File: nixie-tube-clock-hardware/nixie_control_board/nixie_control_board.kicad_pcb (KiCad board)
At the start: 2 copper layers, 52.5 x 97 mm, 67 parts, among them J1 Conn_01x07, J2 Conn_01x02_Female, P1 CONN_01X02, P2 CONN_01X02, P3 AMS1117, P4 CONN_01X02, P5 ., P6 CONN_01X02, P7 CONN_01X02, Q1 IRF644, Q2 Q_PNP_BEC, SW4 SW_DIP_x01, U1 DS3231, U2 AT24C02, U3 MAX1771, U5 DHT11, U6 Logo, U7 SSD1306-OLED, U8 MP2307

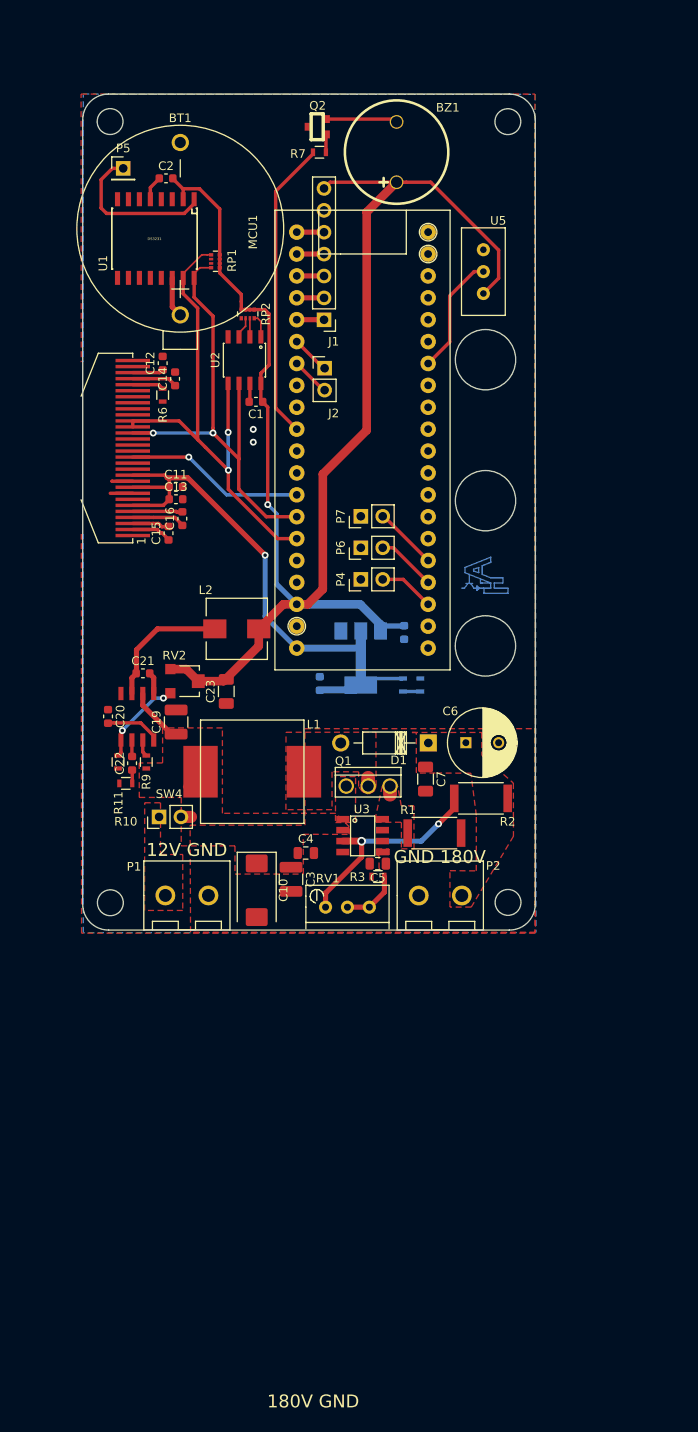
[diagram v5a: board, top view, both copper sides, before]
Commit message: Updated 180V boost supply and updated gitignore
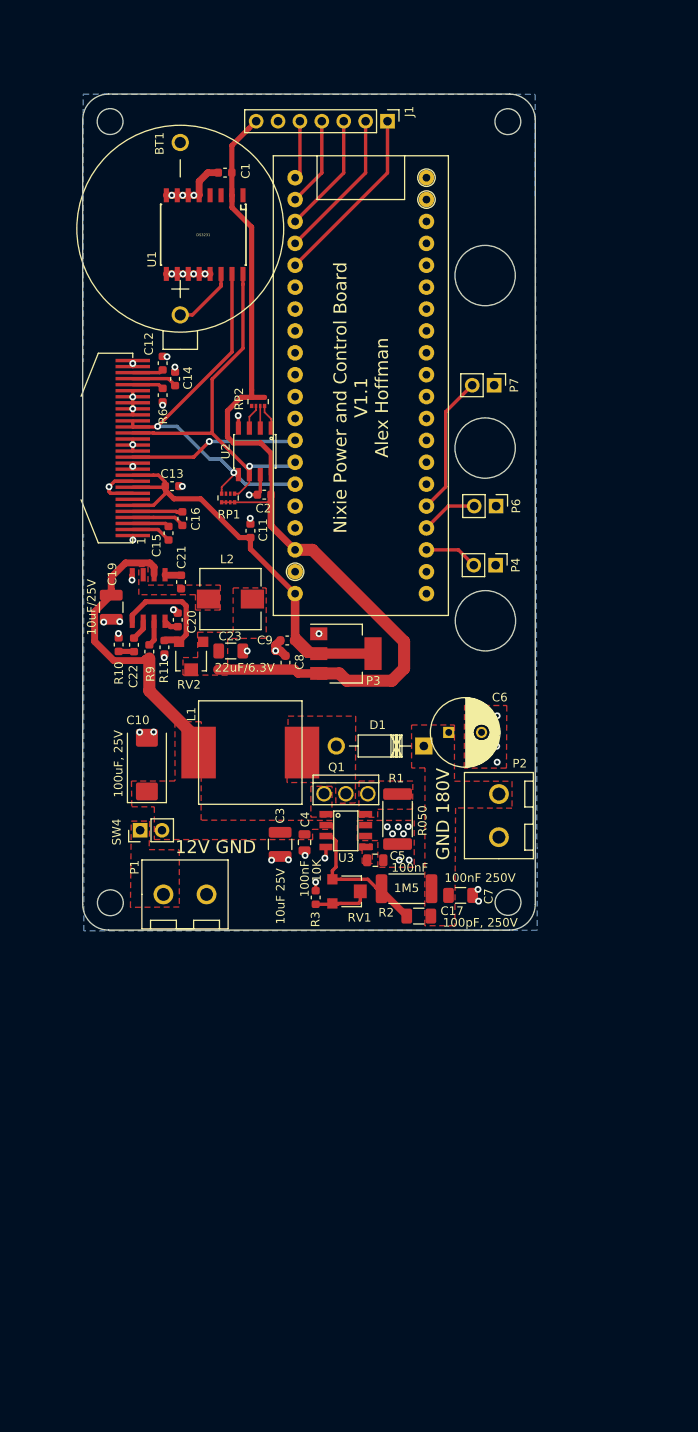
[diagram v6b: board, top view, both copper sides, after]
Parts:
- removed BZ1: Buzzer, keyboard:buzzer
- removed J2: Conn_01x02_Female, Connector_PinHeader_2.54mm:PinHeader_1x02_P2.54mm_Vertical
- removed P5: ., Connector_PinHeader_2.54mm:PinHeader_1x01_P2.54mm_Vertical
- removed Q2: Q_PNP_BEC, keyboard:SOT23-3
- removed R4, R5: 0, Resistors_SMD:R_0603
- removed R7: 1K, Resistors_SMD:R_0603
- removed U5: DHT11, keyboard:DHT11
- removed U6: Logo, keyboard:Logo
- added C17: 100pF, 250V, Capacitor_SMD:C_1206_3216Metric, F.Cu at (159.5, 145.4)
- C3: value 10uF, 25V -> 10uF 25V
- C7: value 100nF, 250V -> 100nF 250V
- C8, C9, P3: moved to F.Cu
- R1: footprint Resistors_SMD:R_2512 -> Resistor_SMD:R_2512_6332Metric
- R10, R11, R3, R6, R9: footprint Resistors_SMD:R_0603 -> Resistor_SMD:R_0603_1608Metric
- R2: value 1M5,220V -> 1M5; footprint Resistors_SMD:R_2512 -> Resistor_SMD:R_2512_6332Metric
- RV1: footprint Potentiometers:Potentiometer_Bourns_3296W_3-8Zoll_Inline_ScrewUp -> Potentiometer_SMD:Potentiometer_Trimmer-EVM3E
- RV2: footprint Potentiometers:Potentiometer_Trimmer-EVM3E -> Potentiometer_SMD:Potentiometer_Trimmer-EVM3E
- SW4: footprint Pin_Headers:Pin_Header_Straight_1x02_Pitch2.54mm -> Connector_PinHeader_2.54mm:PinHeader_1x02_P2.54mm_Vertical
- moved C2 38.4 mm to (141.6, 96.5)
- moved RP1 27.5 mm to (137.4, 96.9), turned to 90 degrees
- moved C1 26.8 mm to (137.0, 59.1)
- moved J1 24.2 mm to (155.9, 53.1), turned to 270 degrees
- moved P7 21.7 mm to (168.3, 83.8), turned to 270 degrees
- moved C10 19.4 mm to (128.0, 127.8), turned to 90 degrees
- moved P6 16.4 mm to (168.5, 97.8), turned to 270 degrees
- moved R10 16.1 mm to (124.7, 113.9), turned to 270 degrees
- moved P4 15.7 mm to (168.4, 104.7), turned to 270 degrees
- moved C19 15.3 mm to (123.8, 109.5), turned to 270 degrees
- moved R11 14.4 mm to (130.0, 114.2)
- moved C8 14.2 mm to (144.0, 116.0), turned to 90 degrees
- moved C7 14.1 mm to (164.4, 143.0), turned to 0 degrees
- moved U8 13.8 mm to (128.2, 108.5)
- moved C20 13.8 mm to (131.6, 111.0)
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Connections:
- MCU1 pad 31: BUZZER -> Net-(MCU1-Pad31)
- MCU1 pad 34: RX -> Net-(MCU1-Pad34)
- MCU1 pad 35: TX -> Net-(MCU1-Pad35)
- MCU1 pad 7: DHT -> Net-(MCU1-Pad7)
- RP1 pad 5: SDA -> SCL
- RP1 pad 8: SCL -> SDA
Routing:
- net +5V: track 178.7 -> 109.6 mm, vias 1 -> 0
- net BUZZER: track 34.9 -> 0.00 mm
- net GND: track 12.1 -> 43.0 mm, vias 2 -> 50
- net +12V: track 11.9 -> 34.5 mm
- net Net-(P5-Pad1): track 18.4 -> 0.00 mm
- net SHIFT_CLEAR: track 3.16 -> 21.2 mm
- net +3V3: track 68.8 -> 52.8 mm, vias 1 -> 0
- net Net-(C21-Pad1): track 15.4 -> 0.00 mm
- net SHIFT_OUT_ENABLE: track 3.16 -> 17.6 mm
- net SDA: track 60.9 -> 46.9 mm
- net DHT: track 13.9 -> 0.00 mm
- net SHIFT_LATCH_CLOCK: track 3.16 -> 14.0 mm
- net BUTTON_3: track 7.39 -> 16.2 mm
- net Net-(BZ1-Pad2): track 8.33 -> 0.00 mm
- net Net-(C17-Pad2): track 25.0 -> 16.8 mm, vias 2 -> 0
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- added copper zone on F.Cu, net +5V
- added copper zone on F.Cu, net Net-(C21-Pad1)
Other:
- board text added: "Nixie Power and Control Board V1.1 Alex Hoffman"
- board text removed: "180V GND"

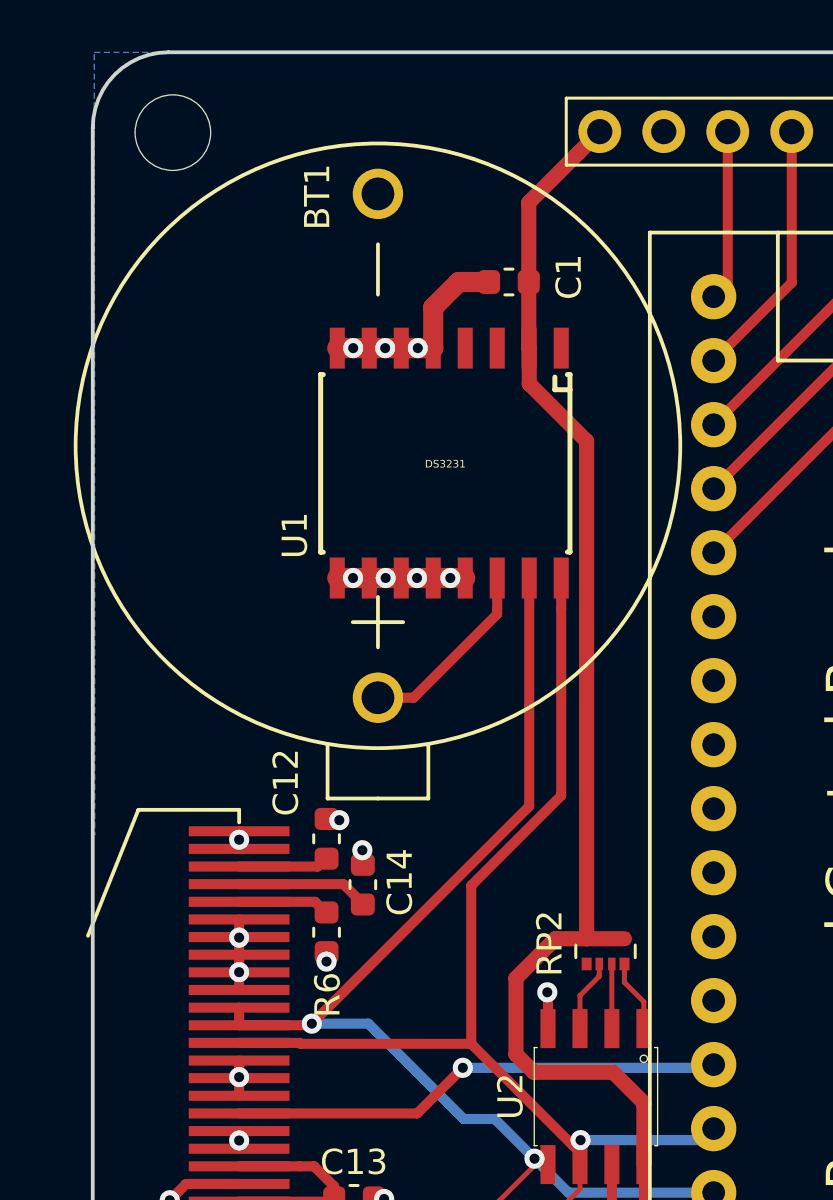
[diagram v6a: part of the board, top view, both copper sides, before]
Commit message: Added empty bluepill project and moved RT clock battery holder
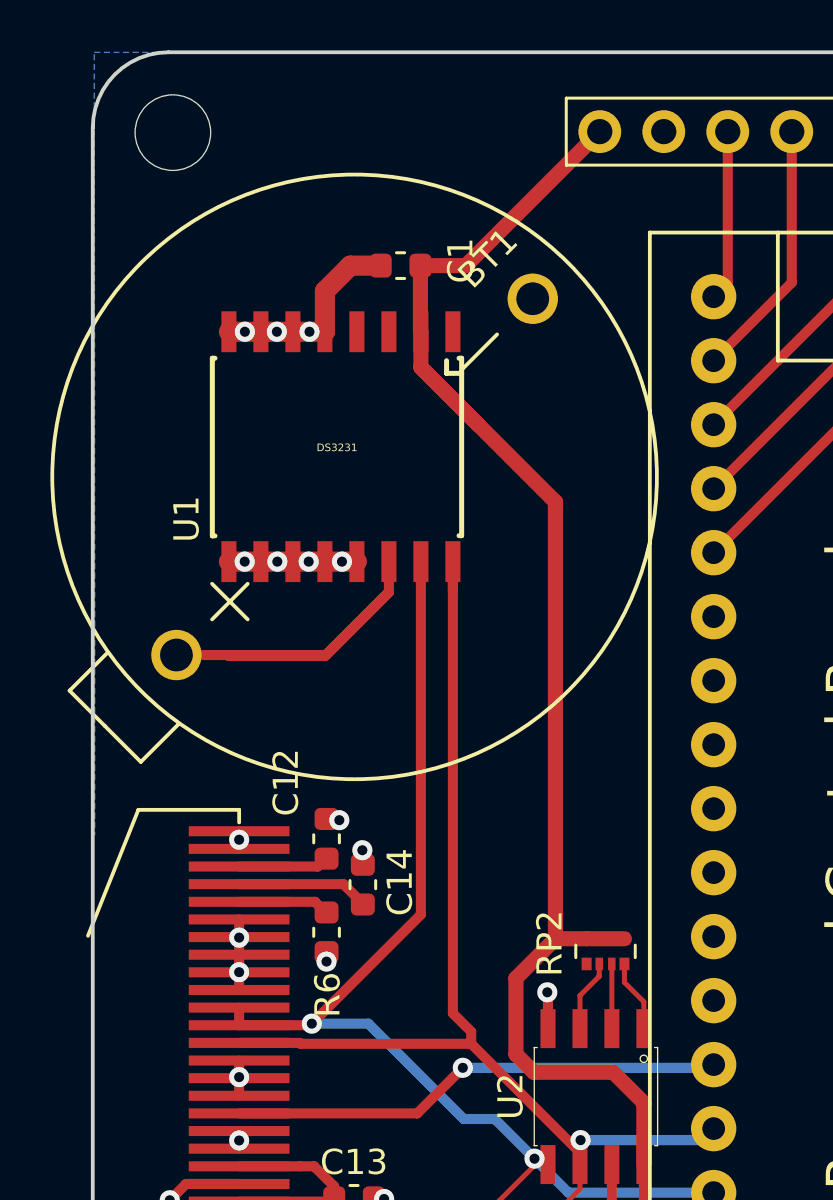
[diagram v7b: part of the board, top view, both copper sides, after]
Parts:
- moved U1 4.35 mm to (130.4, 66.1)
- moved C1 4.35 mm to (132.7, 58.5)
- moved BT1 1.54 mm to (130.9, 66.9), turned to 45 degrees
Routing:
- net Net-(BT1-Pad1): track 7.54 -> 18.1 mm
- net +5V: track 109.6 -> 116.9 mm
- net SDA: track 46.9 -> 45.8 mm
- net SCL: track 60.8 -> 61.5 mm

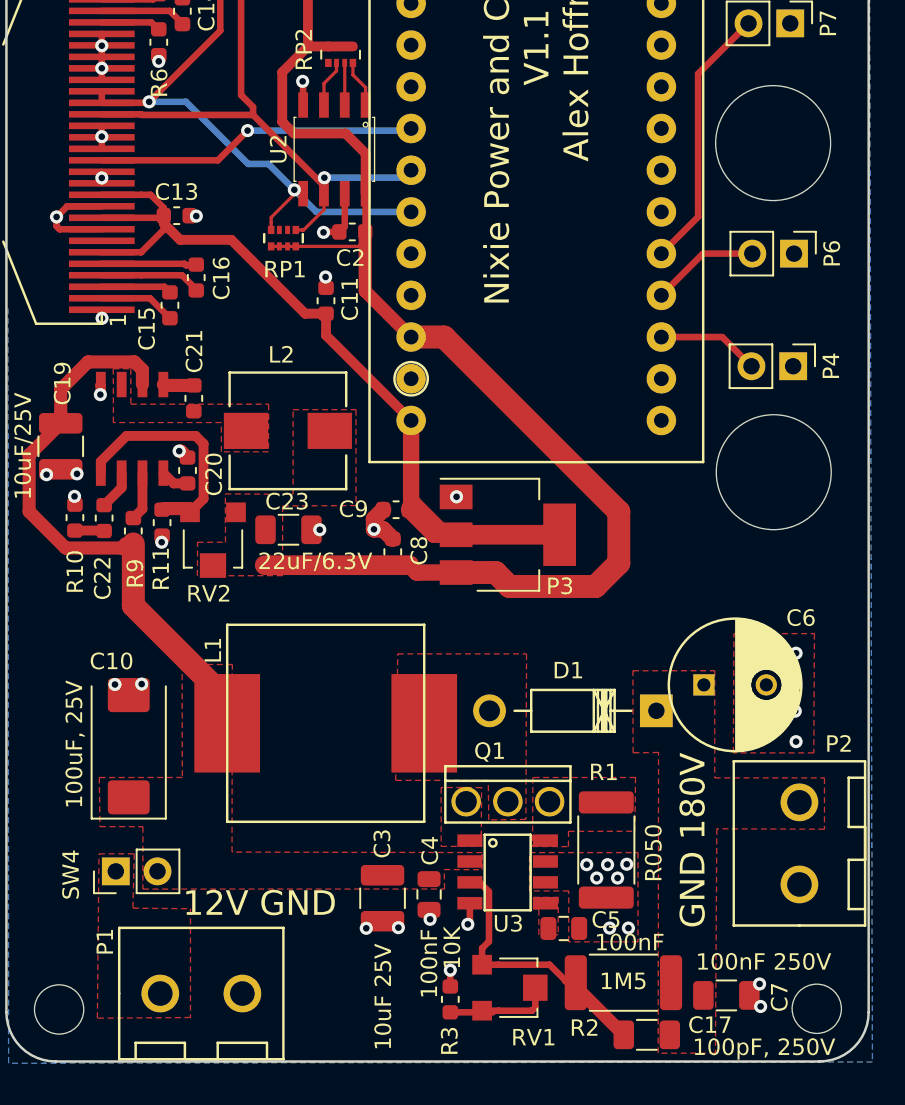
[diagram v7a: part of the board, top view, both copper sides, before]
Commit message: Added pullups to I2C1
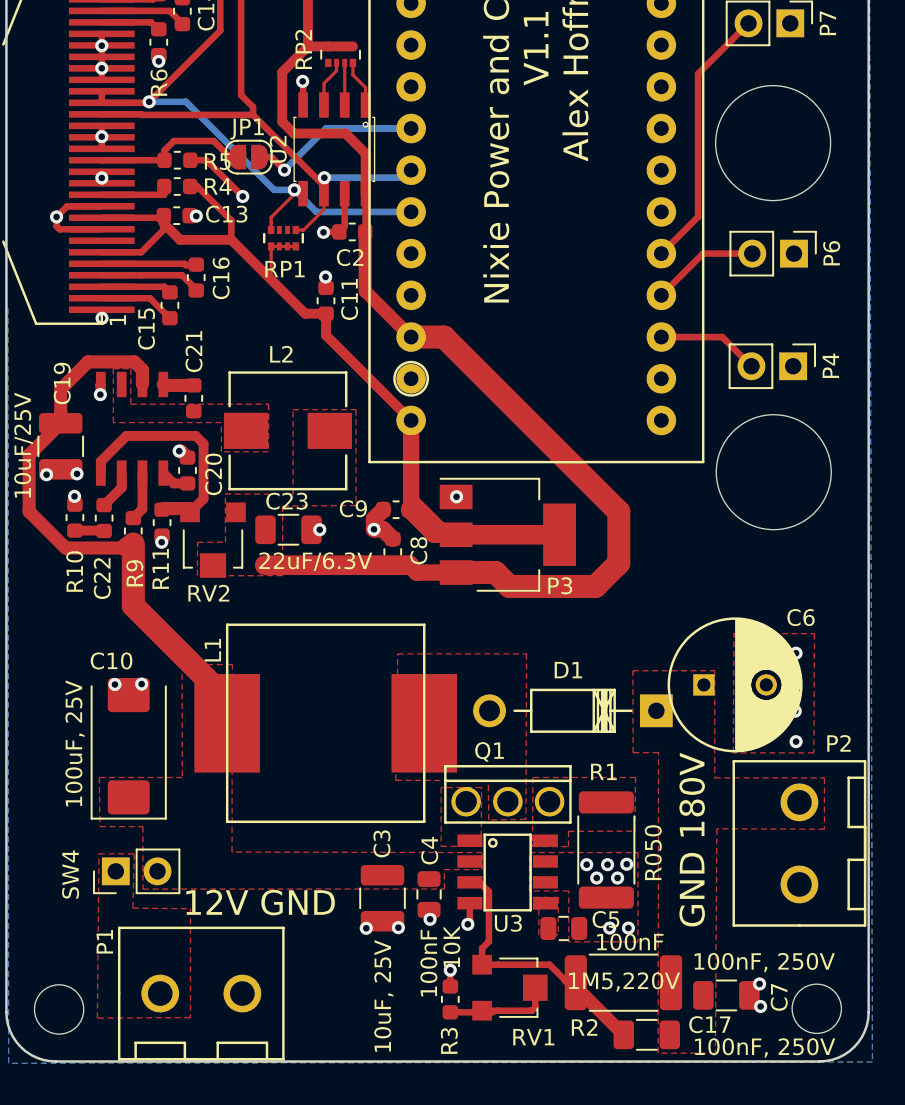
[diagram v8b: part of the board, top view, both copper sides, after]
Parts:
- added JP1: SolderJumper_2_Open, Jumper:SolderJumper-2_P1.3mm_Open_RoundedPad1.0x1.5mm, F.Cu at (135.3, 91.9)
- added R4: 10K, Resistor_SMD:R_0603_1608Metric, F.Cu at (130.9, 93.7)
- added R5: 10K, Resistor_SMD:R_0603_1608Metric, F.Cu at (130.9, 92.1)
- C11, C13, C15, C16: value 1uF -> 2.2uF
- C14: value 2.2uF/16V -> 2.2uF
- C17: value 100pF, 250V -> 100nF, 250V
- C3: value 10uF 25V -> 10uF, 25V
- C7: value 100nF 250V -> 100nF, 250V
- R2: value 1M5 -> 1M5,220V
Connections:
- MCU1 pad 28: DISP_RESET -> /RESET
- RP1 pad 1: +5V -> +3V3
- RP1 pad 2: +5V -> +3V3
- RP1 pad 3: +5V -> +3V3
- RP1 pad 4: +5V -> +3V3
- U7 pad 11: +3V3 -> Net-(R4-Pad2)
- U7 pad 14: DISP_RESET -> Net-(JP1-Pad1)
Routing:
- net DISP_RESET: track 19.6 -> 0.00 mm, vias 1 -> 0
- net /RESET: track 0.00 -> 10.6 mm, vias 0 -> 1
- net Net-(JP1-Pad1): track 0.00 -> 9.53 mm
- net +5V: track 116.9 -> 110.6 mm
- net Net-(R4-Pad2): track 0.00 -> 4.29 mm
- net GND: track 43.0 -> 47.1 mm, vias 50 -> 51
- net +3V3: track 52.8 -> 56.4 mm
